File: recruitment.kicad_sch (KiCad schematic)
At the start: 1 part

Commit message: edited CAD files
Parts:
- removed C1: 1F, Capacitor_SMD:C_0805_2012Metric, symbol Device:C
- added Cbyp1, Cf1: 0,1μF, Capacitor_THT:CP_Axial_L10.0mm_D4.5mm_P15.00mm_Horizontal, symbol Device:C
- added PS1: IH0503SH, Converter_DCDC:Converter_DCDC_XP_POWER-IHxxxxSH_THT, symbol Converter_DCDC:IH0503SH
- added RLA1: G6CU-1114P-US DC5, G6CU-1114P-US-DC5:G6CU-1117P, symbol G6CU-1114P-US-DC5:G6CU-1114P-US_DC5
- added Rf1: 1kΩ, Resistor_THT:R_Axial_DIN0204_L3.6mm_D1.6mm_P5.08mm_Horizontal, symbol Device:R
- added U1: ACS781LLRTR-050B-T, allegro:PSOF7_ACS781LLRTR-050B-T_ALM, symbol allegro:ACS781LLRTR-050B-T
- added U3: ISU0224S05, Converter_DCDC:Converter_DCDC_XP_POWER-ISU02_SMD, symbol Converter_DCDC:ISU0224S05
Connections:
- new net: Rf1.1, U1.3
- new net: RLA1.3, U1.6
- new net 3,3V: Cbyp1.2, U1.1
- new net Earth: Cbyp1.1, Cf1.2, RLA1.1, U1.2
- new net LOAD SUPPLY: RLA1.4
- new net LOAD SYSTEM: U1.5
- new net MONITOR ELECTRONICS/Vcc: RLA1.8
- new net signal: Cf1.1, Rf1.2
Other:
- added sheet MONITOR ELECTRONICS (Monitorcomp.kicad_sch)
- note added: "in 5 out 3"

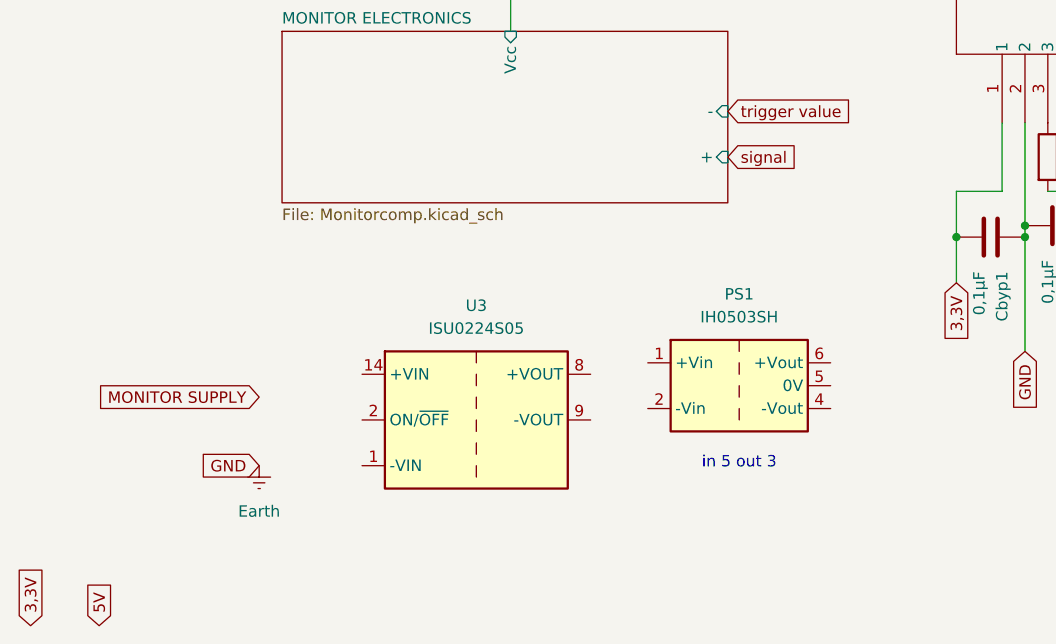
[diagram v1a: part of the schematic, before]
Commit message: DC-DC converter setup
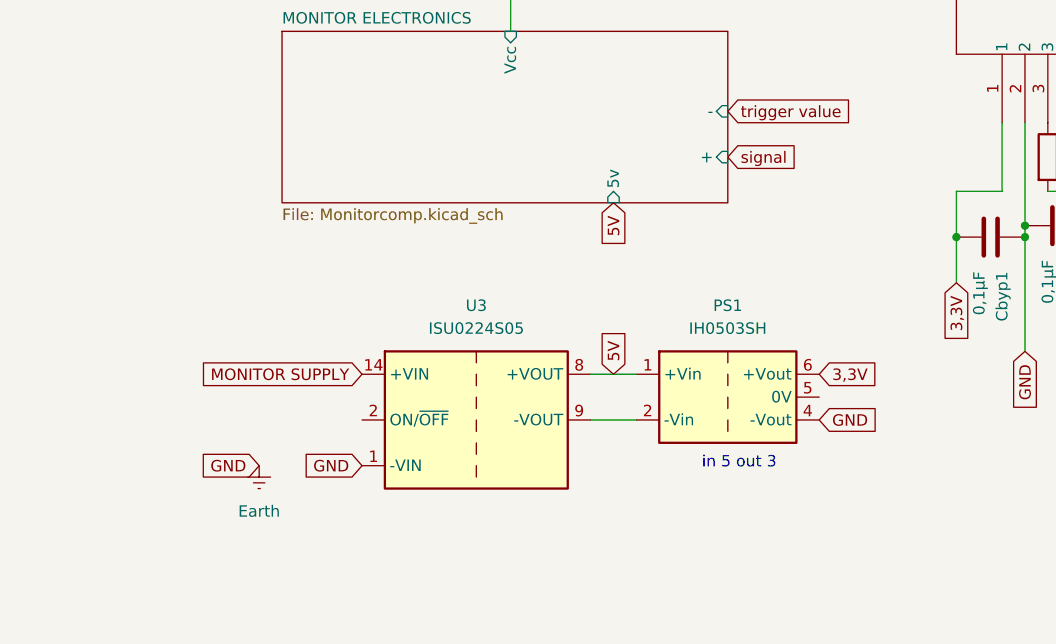
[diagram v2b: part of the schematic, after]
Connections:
- net 3,3V: now also PS1.6 (+Vout)
- net 5V: now also PS1.1 (+Vin), U3.8 (+VOUT)
- net Earth: now also PS1.4 (-Vout), U3.1 (-VIN)
- net MONITOR SUPPLY: now also U3.14 (+VIN)
- net at PS1.2 (-Vin): now also U3.9 (-VOUT)
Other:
- sheet MONITOR ELECTRONICS ports: added 5v; removed none
- moved on the sheet: PS1

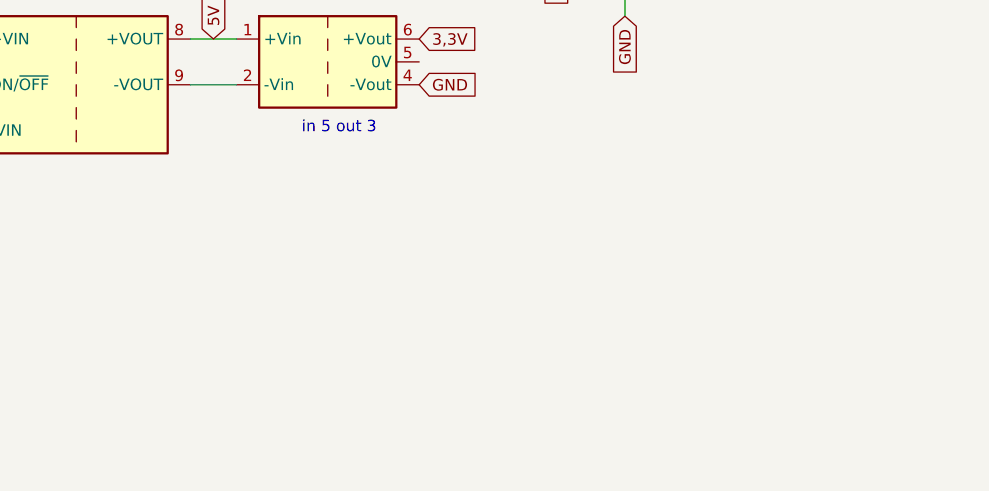
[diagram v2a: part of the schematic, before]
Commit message: LDO integration
added TCR5AM055
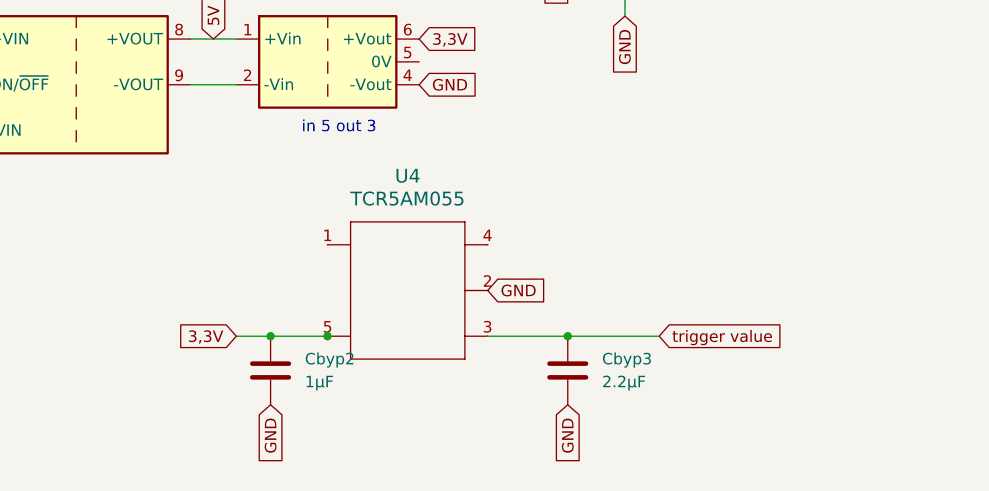
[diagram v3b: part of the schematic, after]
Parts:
- added Cbyp2: 1μF, Capacitor_THT:CP_Axial_L10.0mm_D4.5mm_P15.00mm_Horizontal, symbol Device:C
- added Cbyp3: 2.2μF, Capacitor_THT:CP_Axial_L10.0mm_D4.5mm_P15.00mm_Horizontal, symbol Device:C
- added U4: TCR5AM055, DFN5B_TOS, symbol TCR5AM055:TCR5AM055
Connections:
- net 3,3V: now also Cbyp2.1, U4.5
- net Earth: now also Cbyp2.2, Cbyp3.2
- net trigger value: now also Cbyp3.1

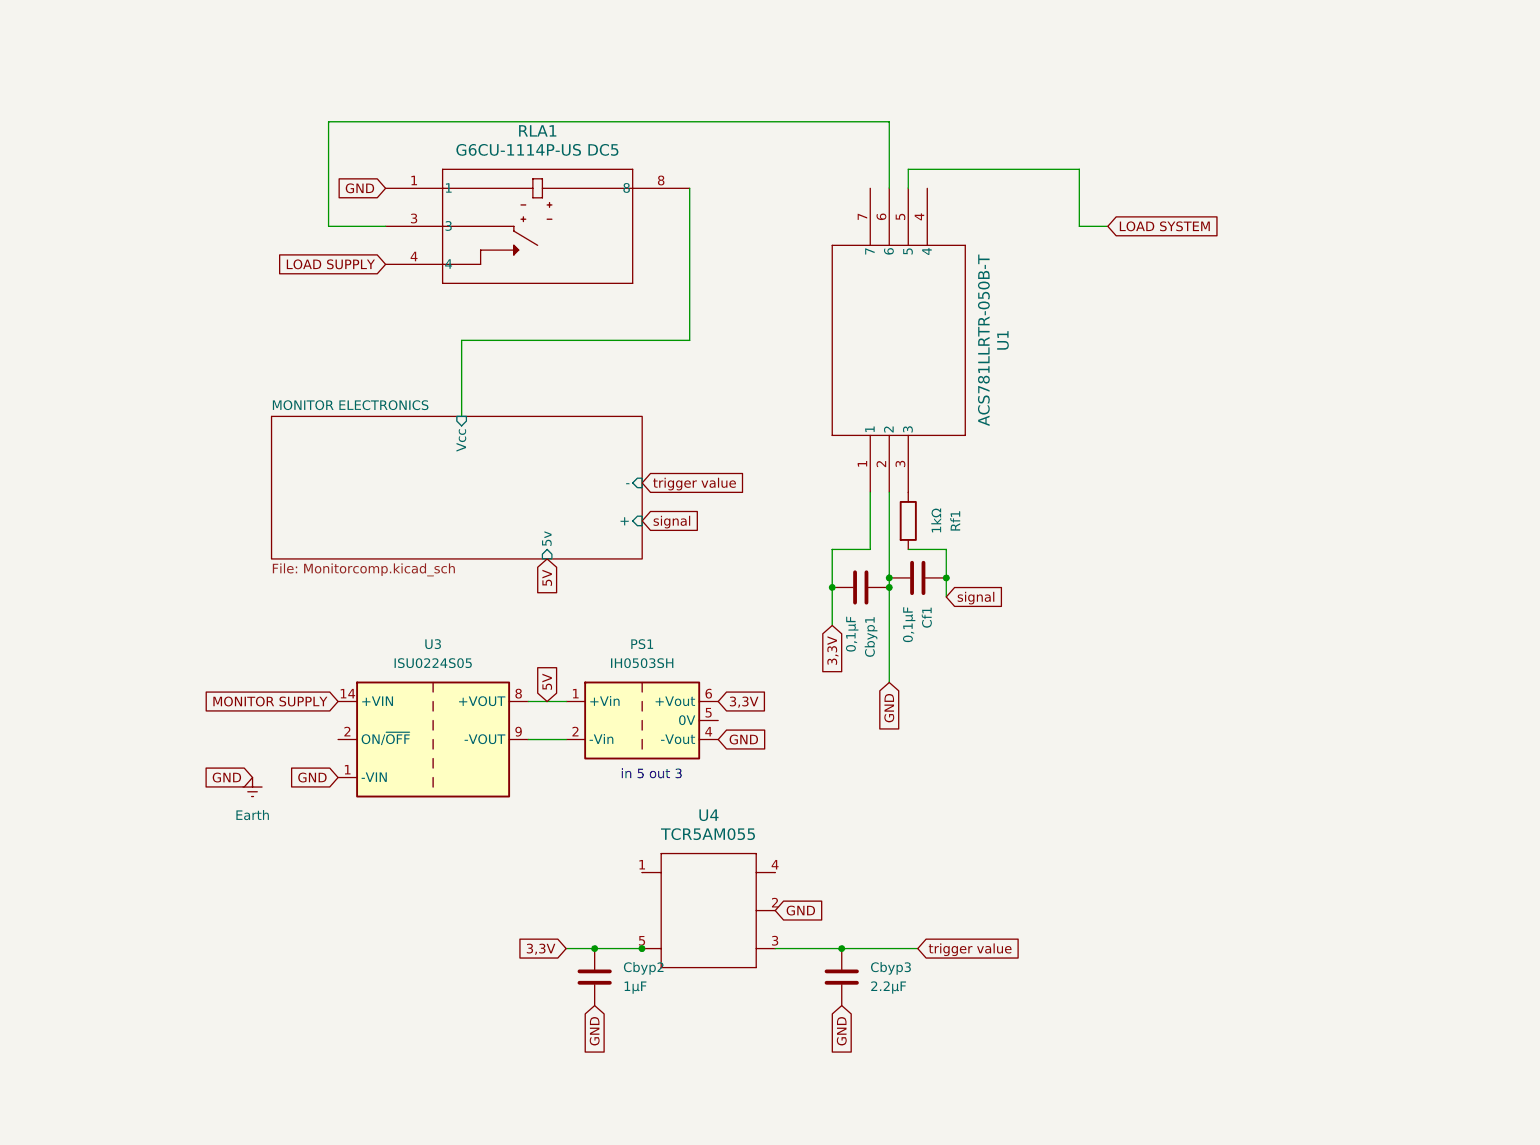
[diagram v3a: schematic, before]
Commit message: edited hierarchical sheets
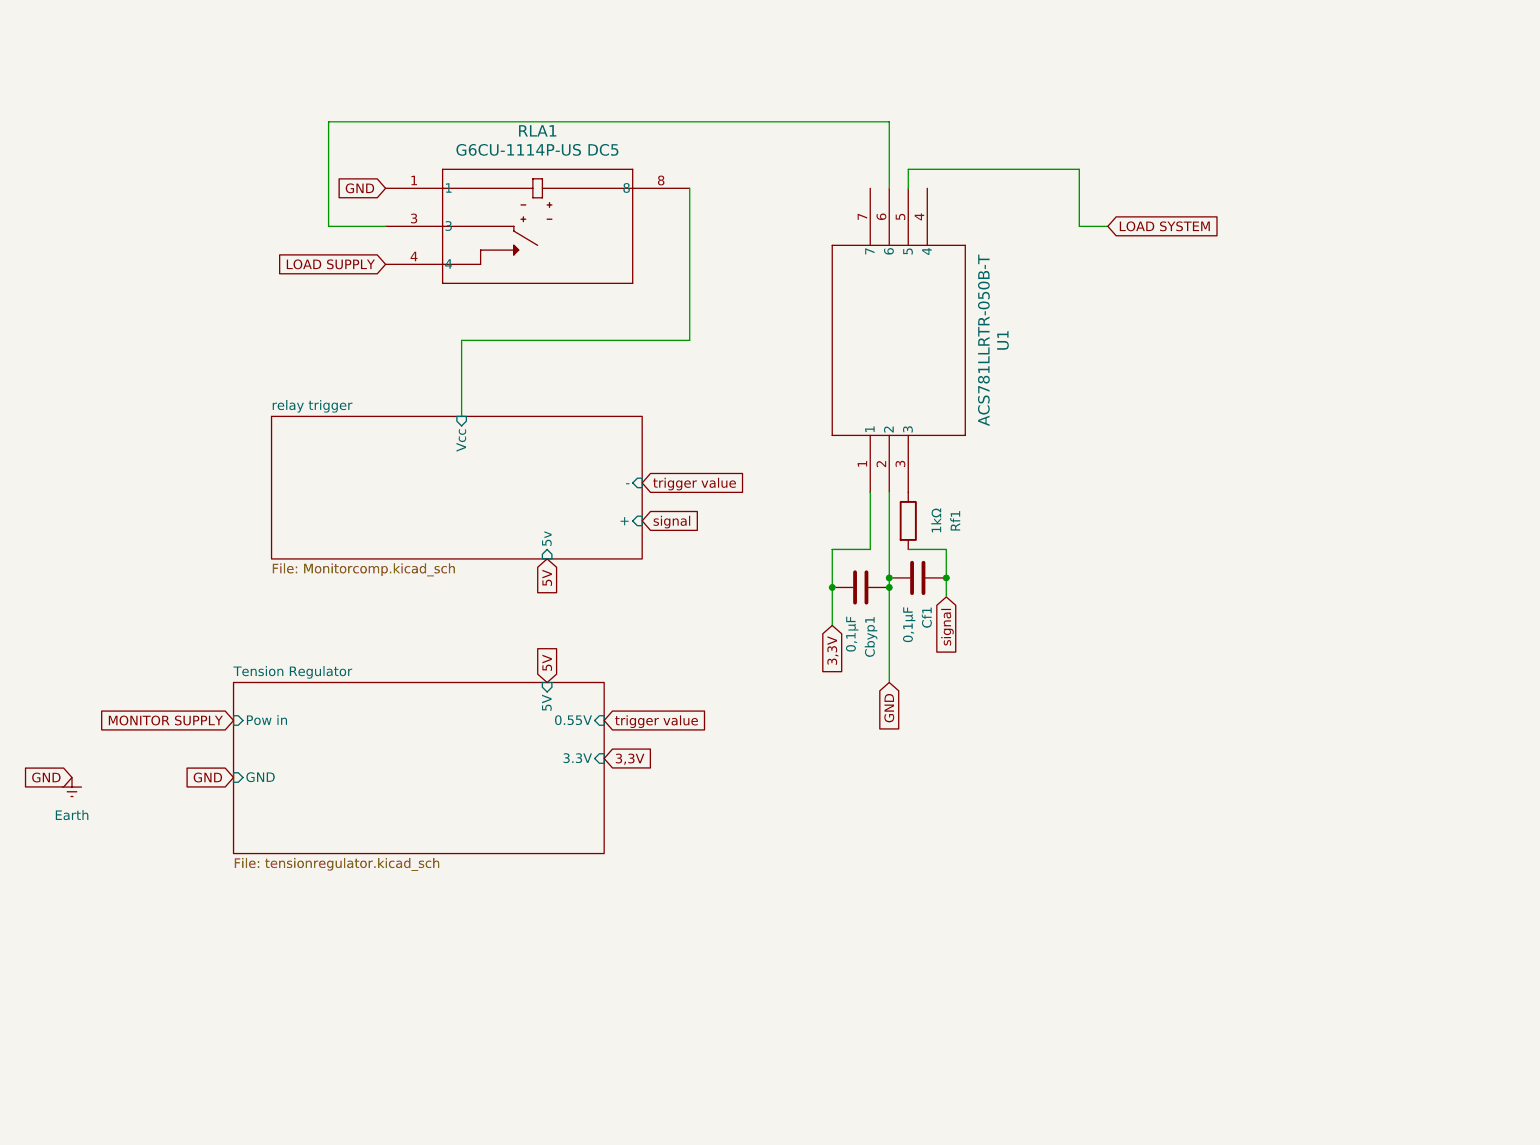
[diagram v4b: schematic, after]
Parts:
- removed Cbyp2: 1μF, Capacitor_THT:CP_Axial_L10.0mm_D4.5mm_P15.00mm_Horizontal, symbol Device:C
- removed Cbyp3: 2.2μF, Capacitor_THT:CP_Axial_L10.0mm_D4.5mm_P15.00mm_Horizontal, symbol Device:C
- removed PS1: IH0503SH, Converter_DCDC:Converter_DCDC_XP_POWER-IHxxxxSH_THT, symbol Converter_DCDC:IH0503SH
- removed U3: ISU0224S05, Converter_DCDC:Converter_DCDC_XP_POWER-ISU02_SMD, symbol Converter_DCDC:ISU0224S05
- removed U4: TCR5AM055, DFN5B_TOS, symbol TCR5AM055:TCR5AM055
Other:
- sheet MONITOR ELECTRONICS renamed relay trigger
- added sheet Tension Regulator (tensionregulator.kicad_sch)
- note removed: "in 5 out 3"

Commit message: fixed relay load distribution
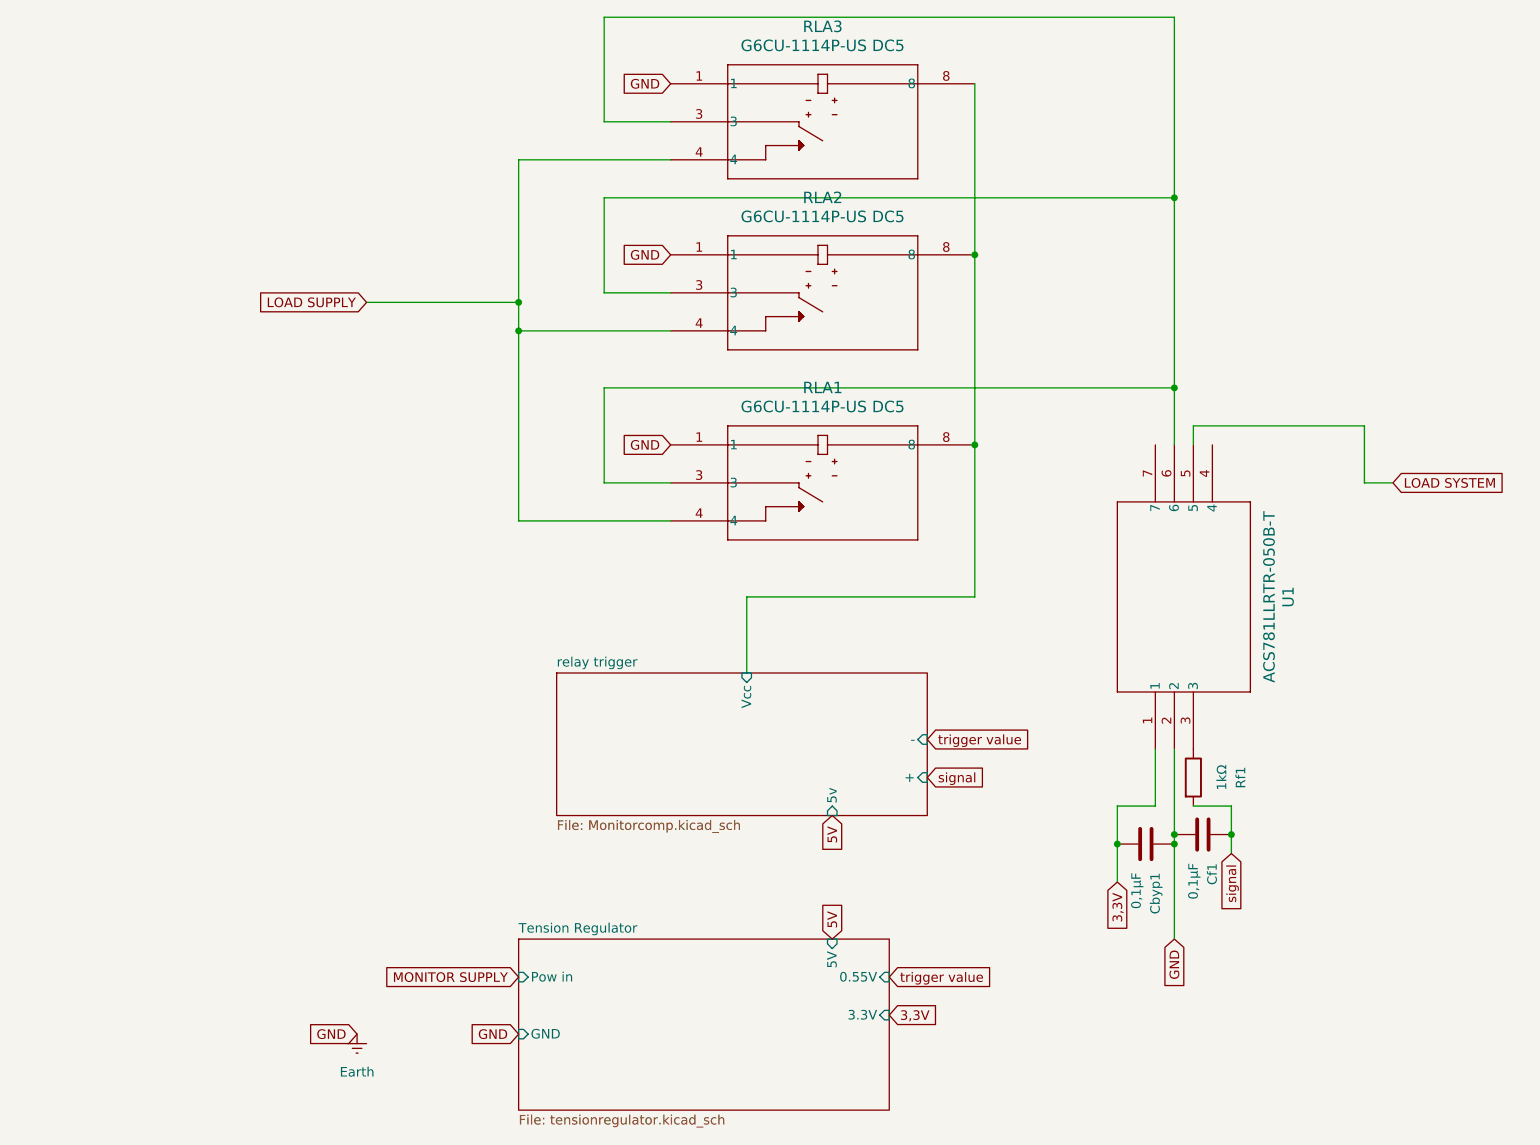
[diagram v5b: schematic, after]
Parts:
- added RLA2, RLA3: G6CU-1114P-US DC5, G6CU-1114P-US-DC5:G6CU-1117P, symbol G6CU-1114P-US-DC5:G6CU-1114P-US_DC5
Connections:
- net Earth: now also RLA2.1, RLA3.1
- net LOAD SUPPLY: now also RLA2.4, RLA3.4
- net relay trigger/Vcc: now also RLA2.8, RLA3.8
- net at RLA1.3, U1.6: now also RLA2.3, RLA3.3
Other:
- moved on the sheet: Cbyp1, Cf1, RLA1, Rf1, U1

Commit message: changed relays
opted for latching dual coil relays,  fixed broken symbols and added a hierarchical sheet
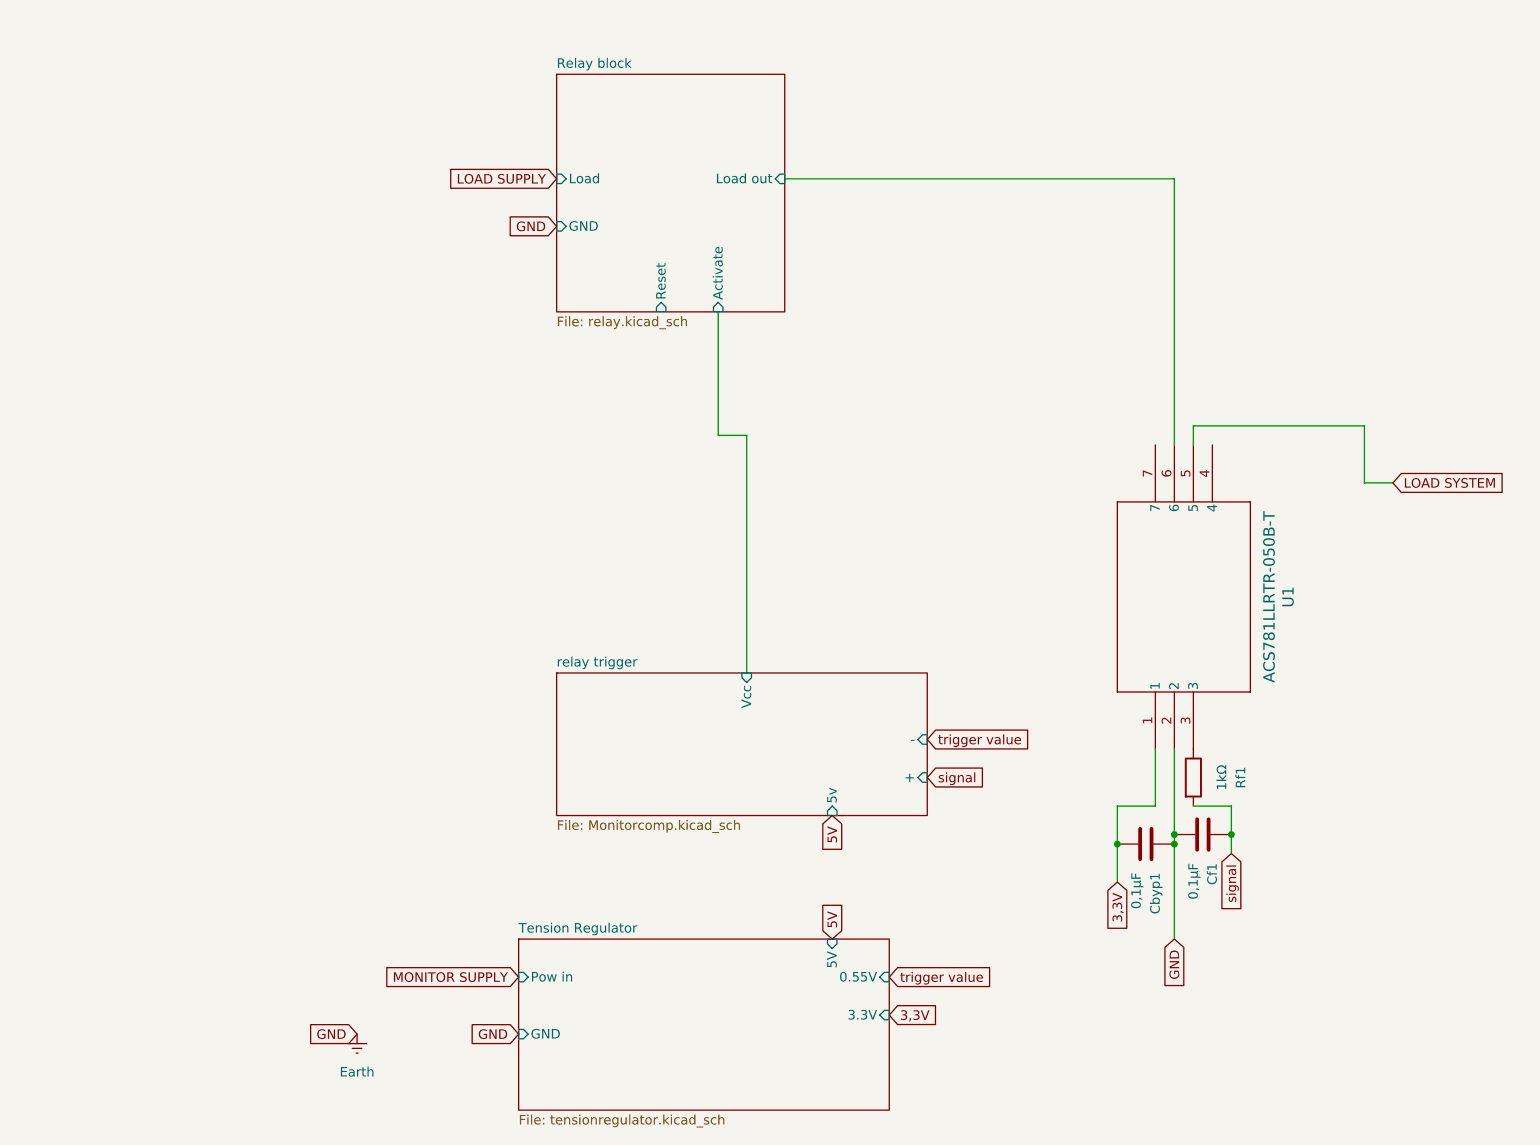
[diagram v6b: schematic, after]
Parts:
- removed RLA1, RLA2, RLA3: G6CU-1114P-US DC5, G6CU-1114P-US-DC5:G6CU-1117P, symbol G6CU-1114P-US-DC5:G6CU-1114P-US_DC5
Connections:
- net Relay block/Load out: now reaches U1.6
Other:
- added sheet Relay block (relay.kicad_sch)
